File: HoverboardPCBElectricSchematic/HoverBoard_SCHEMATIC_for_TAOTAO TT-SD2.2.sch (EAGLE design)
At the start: 60 parts, among them Q3 BC849, Q4 BC849, Q5 BC849, Q6 BC849, Q7 BC849, U1 7805DT, U16 7805DT

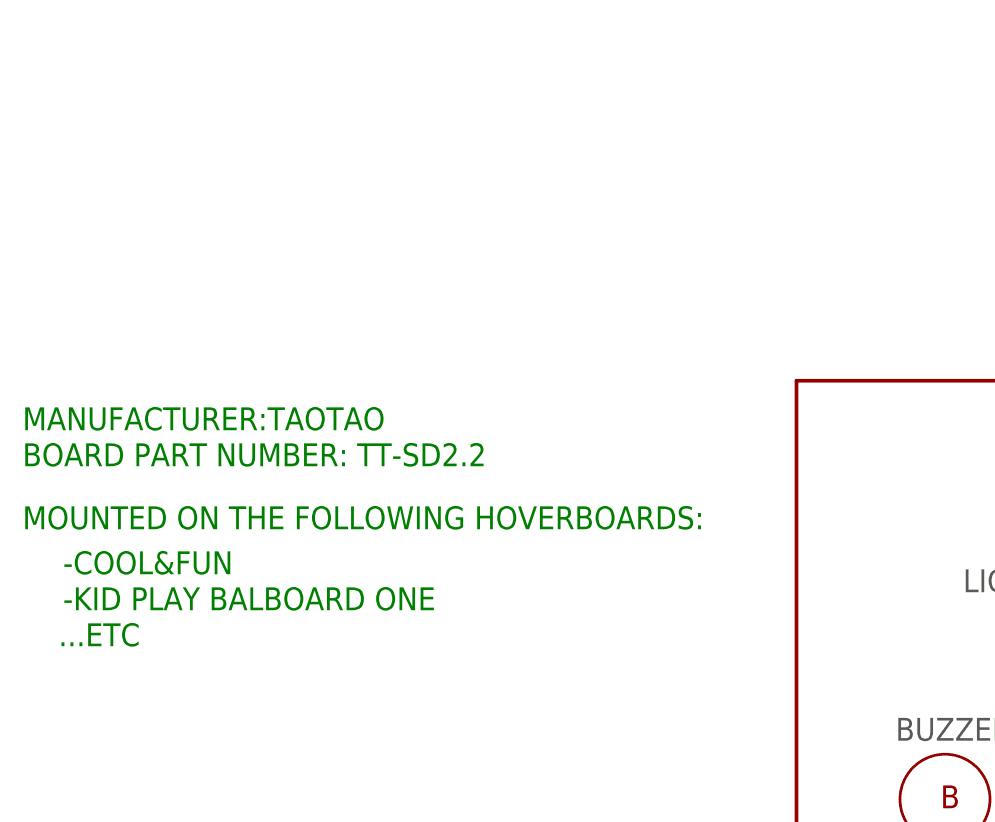
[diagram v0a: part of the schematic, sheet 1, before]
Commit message: accelerometer read
introduced the reading of accelerometer chip to obtain roll and pich (and to shutdown the mower if someone tries to reverse it)
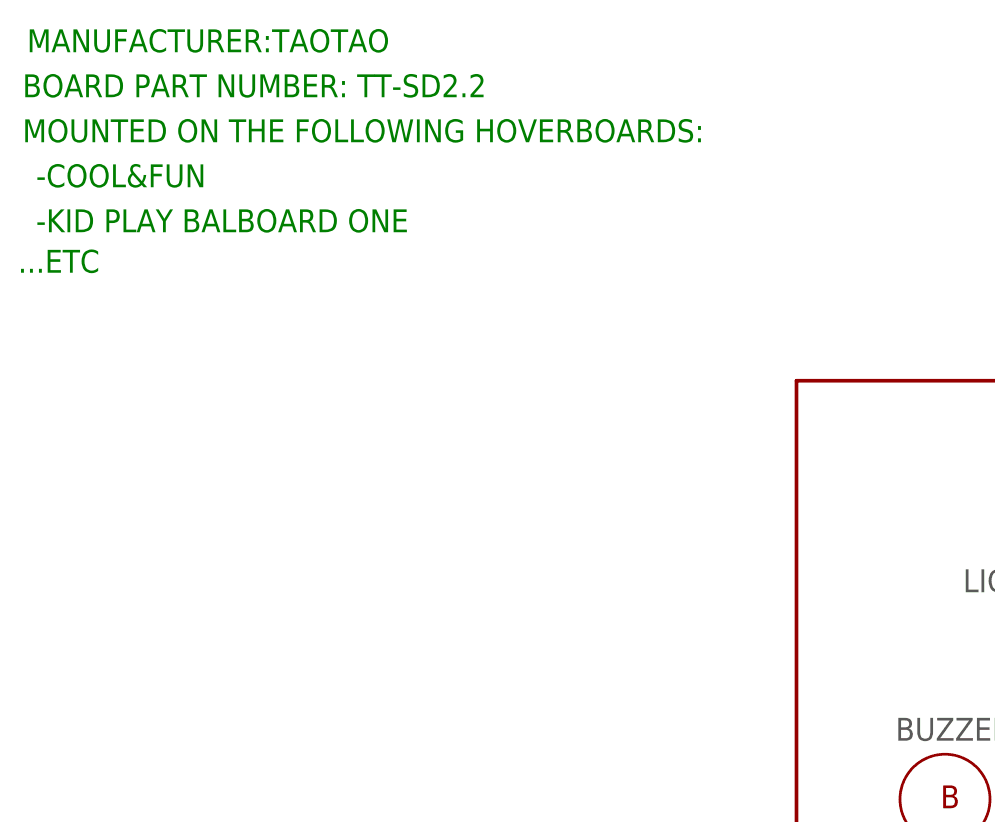
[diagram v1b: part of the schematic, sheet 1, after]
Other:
- note added: "Accelerometer:equivalent to BOSH BMI160 SDA: PB9 (I2C2) SCL: PB8 (I2C2)"
- note added: "U2 MARKING:7NYBS similar to Bosh BMI160 (same pinout and memory structure)"
- note removed: "MPU6050.SDA: PB9 (I2C2) MPU6050.SCL: PB8 (I2C2)"
- note removed: "U2 MARKING:7NYBS ICM-42605"
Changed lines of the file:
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@@
 Y_High: PA8   (out)  TIM0_CH1
 Y_Low : PB13 (out)  TIM0_CH1N</text>
-<text x="120.5" y="148.5" size="2.54" layer="90">V_BATT:                  PA4   (analog)
-CURRENT_DC:        PA6   (analog)
+<text x="101.5" y="150" size="2.54" layer="90">V_BATT:                     PA4   (analog)
+CURRENT_DC:         PA6   (analog)
 EMERGENCY_OFF: PB12 (in)  TIM0_Break_Input
-CHARGE_STATE:    PF0 (in, pullup)
+CHARGE_STATE:     PF0 (in, pullup)
 unused: PB4, PB5, PA6</text>
-<text x="40.5" y="149" size="2.54" layer="90">L1: PA7   (in)
+<text x="21" y="82" size="2.54" layer="90">L1: PA7   (in)
 L2: PA11 (in)
 REMOTE.R: PB7 (I2C1_SDA / USART0_RX)
 REMOTE.T: PB6 (I2C1_SCL / USART0_TX)</text>
-<text x="210" y="162.5" size="2.54" layer="90">MPU6050.SDA: PB9 (I2C2)
-MPU6050.SCL: PB8 (I2C2)</text>
+<text x="187.5" y="161.5" size="2.54" layer="90">Accelerometer:equivalent to BOSH BMI160
+   SDA: PB9 (I2C2)
+   SCL: PB8 (I2C2)</text>
 <wire x1="94" y1="63" x2="94" y2="133" width="0.4064" layer="94"/>
 <wire x1="94" y1="133" x2="243" y2="133" width="0.4064" layer="94"/>
@@
 <text x="158" y="84" size="3.81" layer="91">Controller: GD32F130C8</text>
 <text x="165.44" y="18.82" size="1.778" layer="94">Reverse engineered by Florian and Gaucho</text>
-<text x="8" y="127.5" size="2.54" layer="91">MANUFACTURER:TAOTAO</text>
-<text x="8" y="123.5" size="2.54" layer="91">BOARD PART NUMBER: TT-SD2.2</text>
-<text x="8" y="116.5" size="2.54" layer="91">MOUNTED ON THE FOLLOWING HOVERBOARDS:</text>
-<text x="12.5" y="111.5" size="2.54" layer="91">-COOL&amp;FUN</text>
-<text x="12.5" y="107.5" size="2.54" layer="91">-KID PLAY BALBOARD ONE</text>
-<text x="12" y="103.5" size="2.54" layer="91">...ETC</text>
+<text x="8.5" y="169.5" size="2.54" layer="91">MANUFACTURER:TAOTAO</text>
+<text x="8" y="164.5" size="2.54" layer="91">BOARD PART NUMBER: TT-SD2.2</text>
+<text x="8" y="159.5" size="2.54" layer="91">MOUNTED ON THE FOLLOWING HOVERBOARDS:</text>
+<text x="9.5" y="154.5" size="2.54" layer="91">-COOL&amp;FUN</text>
+<text x="9.5" y="149.5" size="2.54" layer="91">-KID PLAY BALBOARD ONE</text>
+<text x="7.5" y="145" size="2.54" layer="91">...ETC</text>
 </plain>
 <instances>
@@
 <text x="15" y="-8" size="1.778" layer="95">U2
 MARKING:7NYBS
-ICM-42605</text>
+similar to Bosh BMI160
+(same pinout and
+memory structure)</text>
 <text x="13" y="7.5" size="1.778" layer="95">7              6               5</text>
 <text x="13" y="-19.5" size="1.778" layer="95">12            13           14</text>
